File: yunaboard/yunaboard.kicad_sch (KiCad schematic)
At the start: 45 parts, among them J1 USB-C Receptable USB 2.0, J2 JTAG/SWD Tag Connect, J3 PCB ANT, U1 ESP32-S3, U2 CP2102N-Axx-xQFN28, U3 USBLC6-2SC6, U4 MIC5365-3.3YD5, Y1 40 MHz (±10ppm)

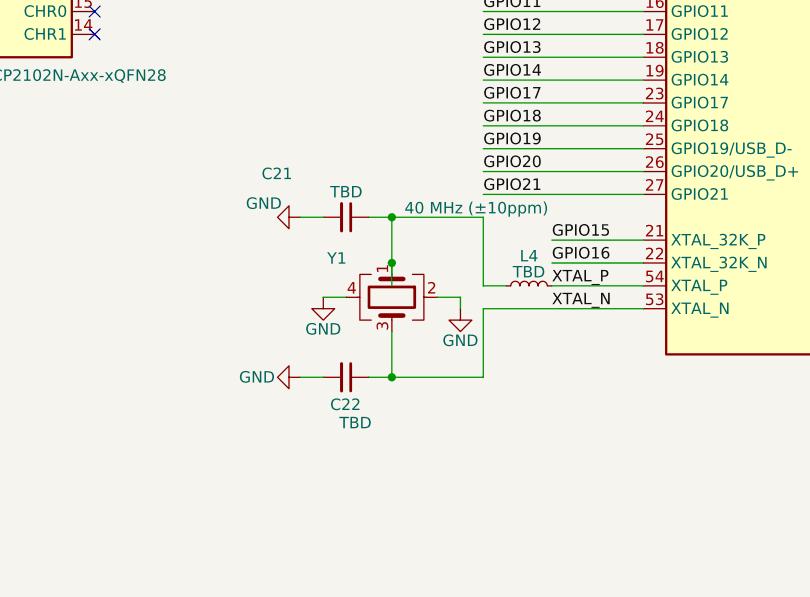
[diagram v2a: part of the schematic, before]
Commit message: Updated
- Added footprints to every component
- Selected capacitors for the external crystals (TBT)
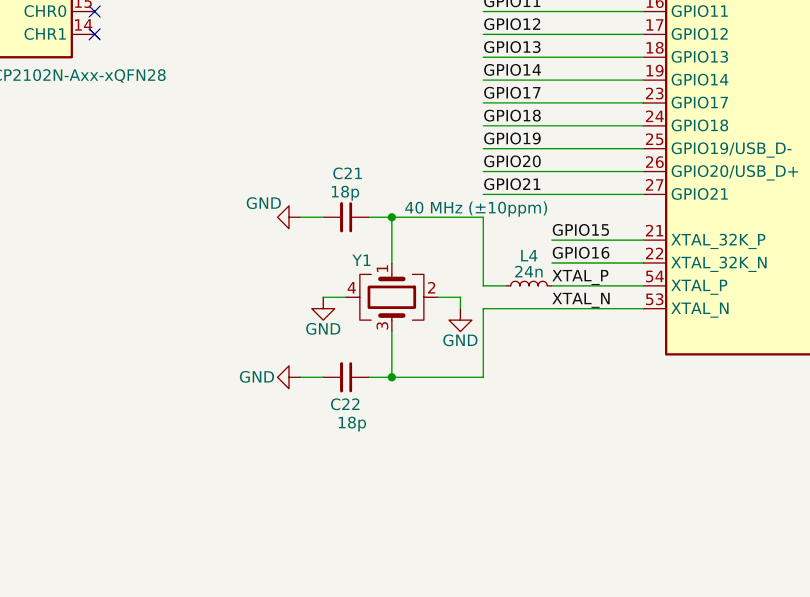
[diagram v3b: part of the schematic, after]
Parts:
- C1, C10, C11, C12, C15, C16, C17, C18, C19, C2, C20, C3, C4, C5, C6: footprint (none) -> Capacitor_SMD:C_0603_1608Metric
- C13, C14, C7, C8, C9: footprint (none) -> Capacitor_SMD:C_0402_1005Metric
- C21, C22: value TBD -> 18p; footprint (none) -> Capacitor_SMD:C_0402_1005Metric
- D1, D2: footprint (none) -> LED_SMD:LED_0603_1608Metric
- J1: footprint (none) -> Connector_USB:USB_C_Receptacle_GCT_USB4105-xx-A_16P_TopMnt_Horizontal
- J3: footprint (none) -> Connector_Coaxial:U.FL_Hirose_U.FL-R-SMT-1_Vertical
- L1, L2, L3: footprint (none) -> Inductor_SMD:L_0201_0603Metric
- L4: value TBD -> 24n; footprint (none) -> Inductor_SMD:L_0201_0603Metric
- R1, R2: footprint (none) -> Resistor_SMD:R_0603_1608Metric
- R3, R4, R5, R6, R7, R8, R9: footprint (none) -> Resistor_SMD:R_0402_1005Metric
- Y1: footprint (none) -> Crystal:Crystal_SMD_3225-4Pin_3.2x2.5mm
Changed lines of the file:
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@@
 	)
 	(junction
-		(at 147.32 127)
-		(diameter 0)
-		(color 0 0 0 0)
-	)
-	(junction
 		(at 33.02 162.56)
 		(diameter 0)
@@
 	(wire
 		(pts
-			(xy 147.32 129.54) (xy 147.32 127)
-		)
-		(stroke
-			(width 0)
-			(type default)
-		)
-	)
-	(wire
-		(pts
 			(xy 45.72 66.04) (xy 48.26 66.04)
 		)
@@
 			)
 		)
-		(property "Footprint" ""
+		(property "Footprint" "Capacitor_SMD:C_0603_1608Metric"
 			(at 142.24 175.26 0)
 			(effects
@@
 			)
 		)
-		(property "Footprint" ""
+		(property "Footprint" "Inductor_SMD:L_0201_0603Metric"
 			(at 137.16 170.18 0)
 			(effects
@@
 			)
 		)
-		(property "Footprint" ""
+		(property "Footprint" "Connector_Coaxial:U.FL_Hirose_U.FL-R-SMT-1_Vertical"
 			(at 165.1 170.18 0)
 			(effects
@@
 			)
 		)
-		(property "Footprint" ""
+		(property "Footprint" "LED_SMD:LED_0603_1608Metric"
 			(at 125.73 73.66 0)
 			(effects
@@
 			)
 		)
-		(property "Footprint" ""
+		(property "Footprint" "Capacitor_SMD:C_0603_1608Metric"
 			(at 187.96 58.42 0)
 			(effects
@@
 			)
 		)
-		(property "Footprint" ""
+		(property "Footprint" "Capacitor_SMD:C_0603_1608Metric"
 			(at 71.12 167.64 0)
 			(effects
@@
 			)
 		)
-		(property "Footprint" ""
+		(property "Footprint" "Capacitor_SMD:C_0603_1608Metric"
 			(at 33.02 167.64 0)
 			(effects
@@
 			)
 		)
-		(property "Footprint" ""
+		(property "Footprint" "Connector_USB:USB_C_Receptacle_GCT_USB4105-xx-A_16P_TopMnt_Horizontal"
 			(at 34.29 73.66 0)
 			(effects
@@
 			)
 		)
-		(property "Footprint" ""
+		(property "Footprint" "Capacitor_SMD:C_0402_1005Metric"
 			(at 180.34 40.64 0)
 			(effects
@@
 		(dnp no)
 		(property "Reference" "Y1"
-			(at 141.224 126.492 90)
+			(at 144.018 126.746 90)
 			(effects
 				(font
@@
 			)
 		)
-		(property "Footprint" ""
+		(property "Footprint" "Crystal:Crystal_SMD_3225-4Pin_3.2x2.5mm"
 			(at 147.32 130.81 0)
 			(effects
@@
 			)
 		)
-		(property "Footprint" ""
+		(property "Footprint" "Capacitor_SMD:C_0402_1005Metric"
 			(at 203.2 35.56 0)
 			(effects
@@
 			)
 		)
-		(property "Footprint" ""
+		(property "Footprint" "Resistor_SMD:R_0603_1608Metric"
 			(at 50.8 63.5 0)
 			(effects
@@
 			)
 		)
-		(property "Footprint" ""
+		(property "Footprint" "Capacitor_SMD:C_0402_1005Metric"
 			(at 220.98 60.96 0)
 			(effects
@@
 			)
 		)
-		(property "Footprint" ""
+		(property "Footprint" "Capacitor_SMD:C_0603_1608Metric"
 			(at 213.36 48.26 0)
 			(effects
@@
 			)
 		)
-		(property "Footprint" ""
+		(property "Footprint" "Capacitor_SMD:C_0402_1005Metric"
 			(at 205.74 48.26 0)
 			(effects
@@
 			)
 		)
-		(property "Footprint" ""
+		(property "Footprint" "Resistor_SMD:R_0402_1005Metric"
 			(at 137.16 73.66 0)
 			(effects
@@
 			)
 		)
-		(property "Footprint" ""
+		(property "Footprint" "Capacitor_SMD:C_0603_1608Metric"
 			(at 152.4 182.88 0)
 			(effects
@@
 			)
 		)
-		(property "Footprint" ""
+		(property "Footprint" "Inductor_SMD:L_0201_0603Metric"
 			(at 152.4 175.26 0)
 			(effects
@@
 			)
 		)
-		(property "Footprint" ""
+		(property "Footprint" "Capacitor_SMD:C_0603_1608Metric"
 			(at 114.3 33.02 0)
 			(effects
@@
 			)
 		)
-		(property "Footprint" ""
+		(property "Footprint" "Capacitor_SMD:C_0603_1608Metric"
 			(at 246.38 139.7 0)
 			(effects
@@
 			)
 		)
-		(property "Footprint" ""
+		(property "Footprint" "Capacitor_SMD:C_0402_1005Metric"
 			(at 190.5 40.64 0)
 			(effects
@@
 			)
 		)
-		(property "Footprint" ""
+		(property "Footprint" "Capacitor_SMD:C_0603_1608Metric"
 			(at 180.34 58.42 0)
 			(effects
@@
 			)
 		)
-		(property "Footprint" ""
+		(property "Footprint" "LED_SMD:LED_0603_1608Metric"
 			(at 125.73 78.74 0)
 			(effects
@@
 			)
 		)
-		(property "Footprint" ""
+		(property "Footprint" "Resistor_SMD:R_0603_1608Metric"
 			(at 50.8 66.04 0)
 			(effects
@@
 			)
 		)
-		(property "Footprint" ""
+		(property "Footprint" "Capacitor_SMD:C_0603_1608Metric"
 			(at 129.54 175.26 0)
 			(effects
@@
 			)
 		)
-		(property "Footprint" ""
+		(property "Footprint" "Capacitor_SMD:C_0603_1608Metric"
 			(at 40.64 167.64 0)
 			(effects
@@
 			)
 		)
-		(property "Footprint" ""
+		(property "Footprint" "Resistor_SMD:R_0402_1005Metric"
 			(at 78.74 45.72 0)
 			(effects
@@
 			)
 		)
-		(property "Footprint" ""
+		(property "Footprint" "Resistor_SMD:R_0402_1005Metric"
 			(at 27.94 162.56 0)
 			(effects
@@
 			)
 		)
-		(property "Value" "TBD"
+		(property "Value" "24n"
 			(at 162.56 128.016 90)
 			(effects
@@
 			)
 		)
-		(property "Footprint" ""
+		(property "Footprint" "Inductor_SMD:L_0201_0603Metric"
 			(at 162.56 129.54 0)
 			(effects
@@
 			)
 		)
-		(property "Footprint" ""
+		(property "Footprint" "Capacitor_SMD:C_0603_1608Metric"
 			(at 175.26 40.64 0)
 			(effects
@@
 			)
 		)
-		(property "Footprint" ""
+		(property "Footprint" "Resistor_SMD:R_0402_1005Metric"
 			(at 246.38 129.54 0)
 			(effects
@@
 			)
 		)
-		(property "Footprint" ""
+		(property "Footprint" "Inductor_SMD:L_0201_0603Metric"
 			(at 185.42 35.56 0)
 			(effects
@@
 			)
 		)
-		(property "Footprint" ""
+		(property "Footprint" "Resistor_SMD:R_0402_1005Metric"
 			(at 137.16 78.74 0)
 			(effects
@@
 			)
 		)
-		(property "Footprint" ""
+		(property "Footprint" "Capacitor_SMD:C_0603_1608Metric"
 			(at 22.86 167.64 0)
 			(effects
@@
 		(dnp no)
 		(property "Reference" "C21"
-			(at 132.842 117.094 90)
+			(at 140.716 117.094 90)
 			(effects
 				(font
@@
 			)
 		)
-		(property "Value" "TBD"
+		(property "Value" "18p"
 			(at 140.462 119.126 90)
 			(effects
@@
 			)
 		)
-		(property "Footprint" ""
+		(property "Footprint" "Capacitor_SMD:C_0402_1005Metric"
 			(at 142.24 121.92 0)
 			(effects
@@
 			)
 		)
-		(property "Footprint" ""
+		(property "Footprint" "Resistor_SMD:R_0402_1005Metric"
 			(at 86.36 40.64 0)
 			(effects
@@
 			)
 		)
-		(property "Value" "TBD"
-			(at 141.478 144.78 90)
+		(property "Value" "18p"
+			(at 141.224 144.78 90)
 			(effects
 				(font
@@
 			)
 		)
-		(property "Footprint" ""
+		(property "Footprint" "Capacitor_SMD:C_0402_1005Metric"
 			(at 142.24 139.7 0)
 			(effects
@@
 			)
 		)
-		(property "Footprint" ""
+		(property "Footprint" "Resistor_SMD:R_0402_1005Metric"
 			(at 78.74 55.88 0)
 			(effects
@@
 			)
 		)
-		(property "Footprint" ""
+		(property "Footprint" "Capacitor_SMD:C_0603_1608Metric"
 			(at 170.18 40.64 0)
 			(effects
@@
 			)
 		)
-		(property "Footprint" ""
+		(property "Footprint" "Capacitor_SMD:C_0603_1608Metric"
 			(at 106.68 33.02 0)
 			(effects

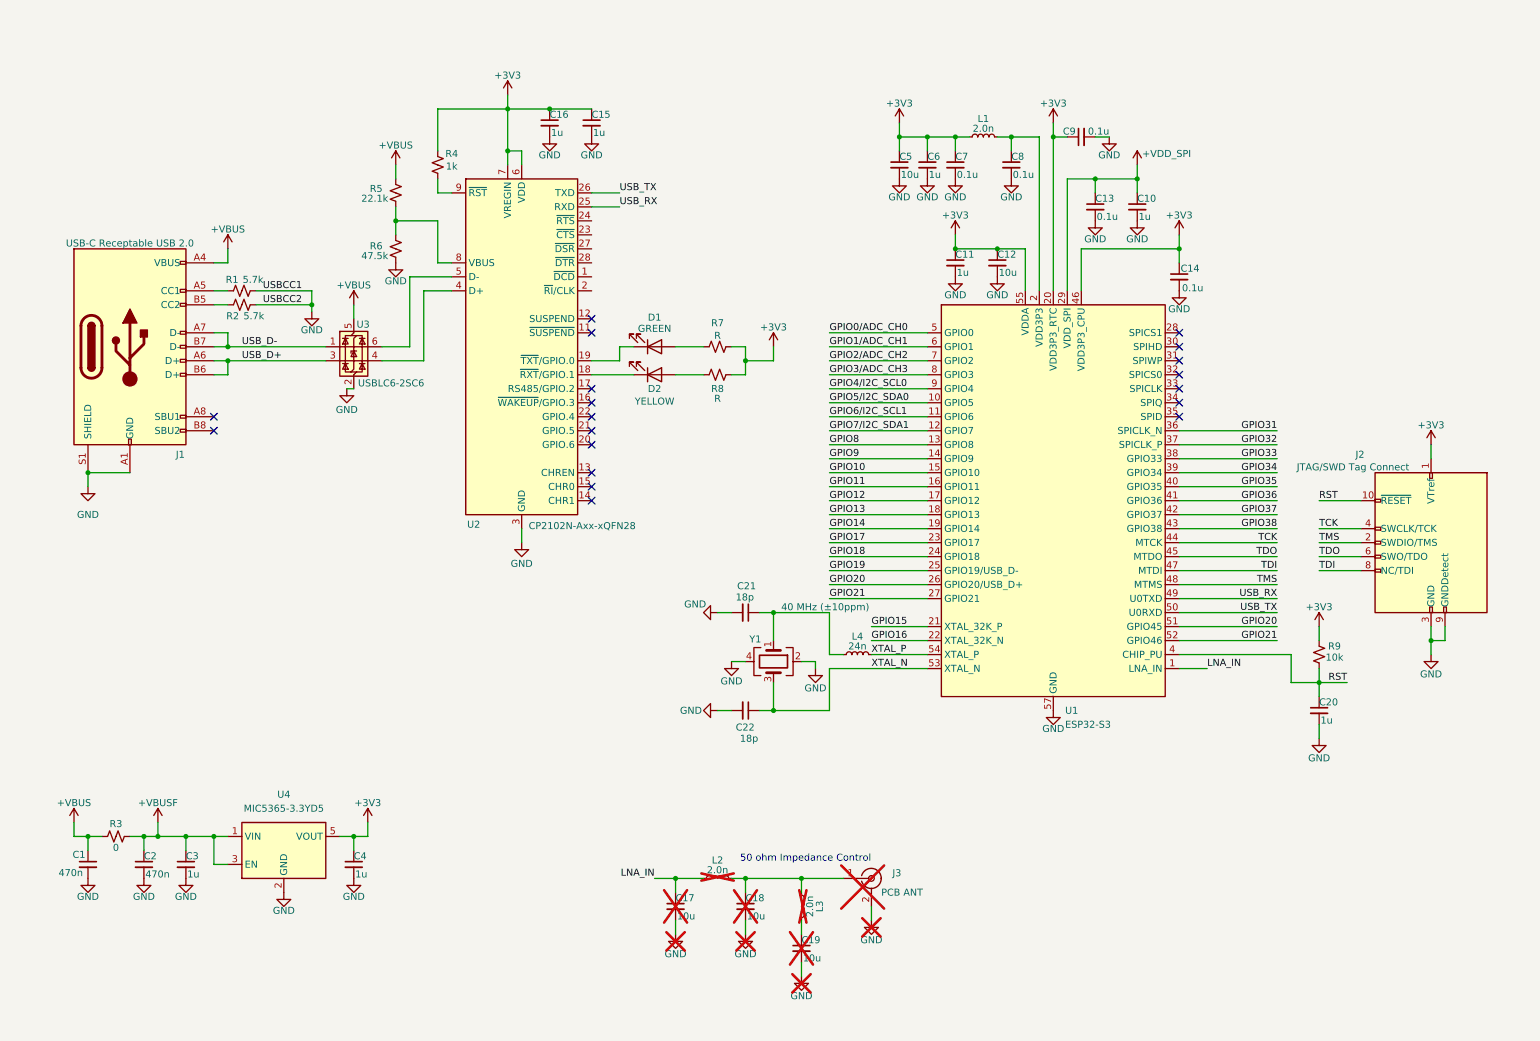
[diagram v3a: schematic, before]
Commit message: Update
- Added GPIO pin headers
- Excluded RF antenna  portion (LNA_IN) - may add in the future
- Started initial PCB layout
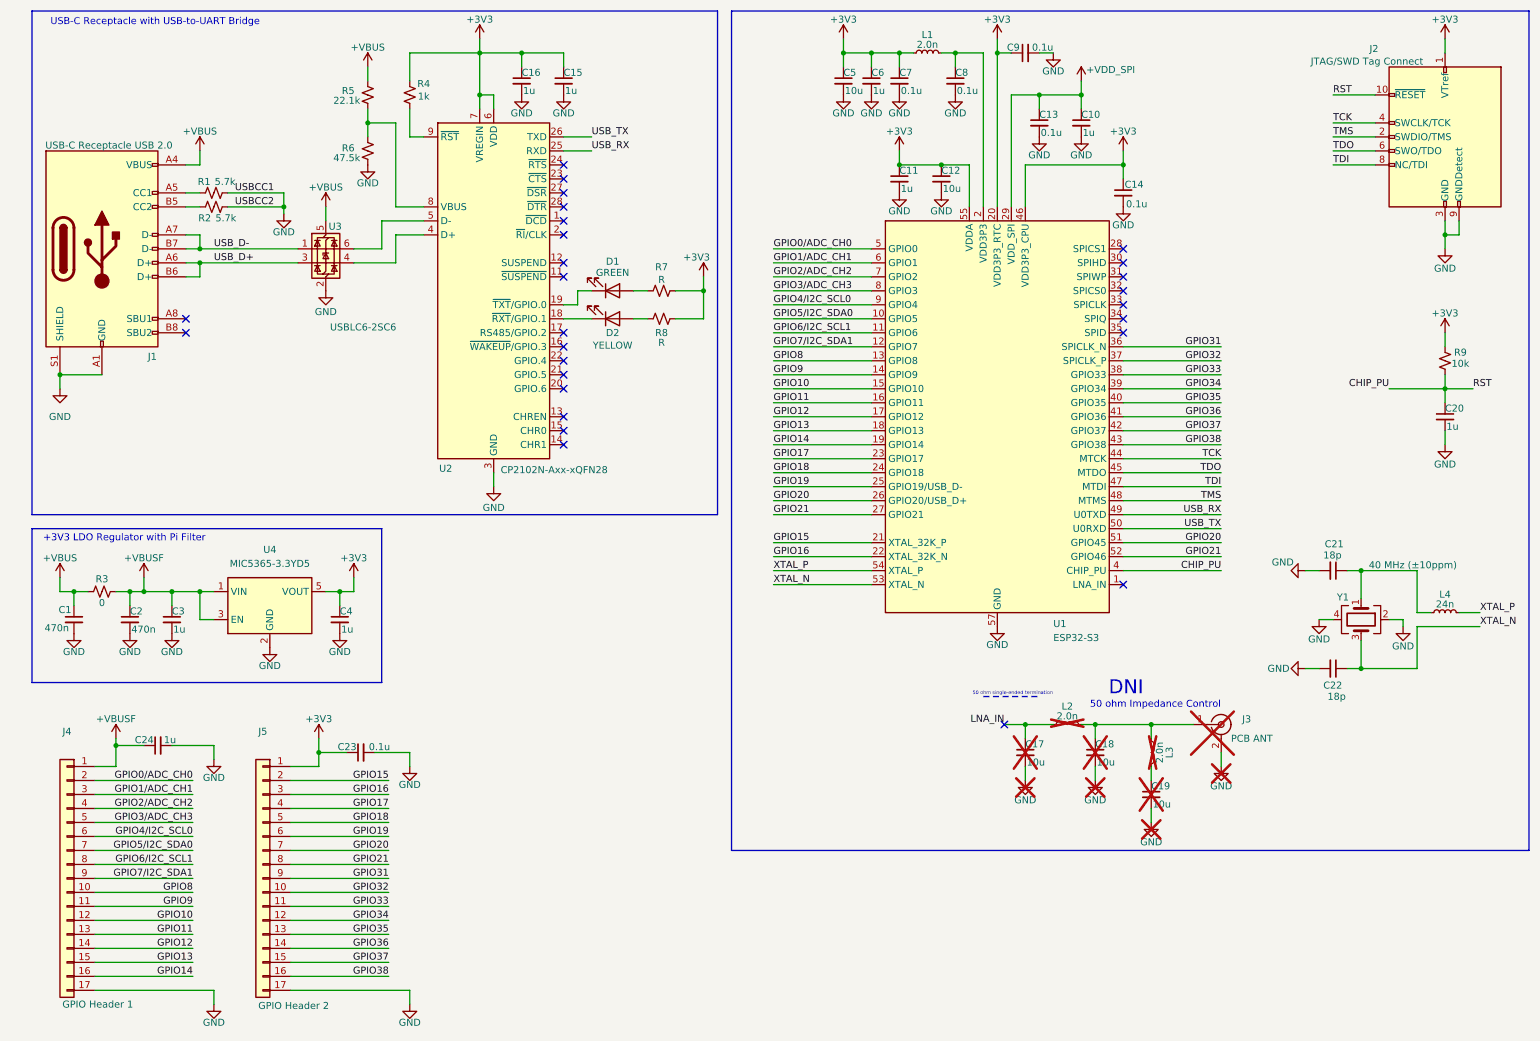
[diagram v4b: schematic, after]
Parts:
- added C23: 0.1u, Capacitor_SMD:C_0402_1005Metric, symbol Device:C_Small
- added C24: 1u, Capacitor_SMD:C_0402_1005Metric, symbol Device:C_Small
- added J4: GPIO Header 1, Connector_PinHeader_1.00mm:PinHeader_1x17_P1.00mm_Vertical, symbol Connector_Generic:Conn_01x17
- added J5: GPIO Header 2, Connector_PinHeader_1.00mm:PinHeader_1x17_P1.00mm_Vertical, symbol Connector_Generic:Conn_01x17
- J1: value USB-C Receptable USB 2.0 -> USB-C Receptacle USB 2.0
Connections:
- net +3V3: now also C23.1, J5.1 (Pin_1)
- net +VBUSF: now also C24.1, J4.1 (Pin_1)
- net GND: now also C23.2, C24.2, J4.17 (Pin_17), J5.17 (Pin_17)
- net GPIO0/ADC_CH0: now also J4.2 (Pin_2)
- net GPIO10: now also J4.12 (Pin_12)
- net GPIO11: now also J4.13 (Pin_13)
- net GPIO12: now also J4.14 (Pin_14)
- net GPIO13: now also J4.15 (Pin_15)
- net GPIO14: now also J4.16 (Pin_16)
- net GPIO15: now also J5.2 (Pin_2)
- net GPIO16: now also J5.3 (Pin_3)
- net GPIO17: now also J5.4 (Pin_4)
- net GPIO18: now also J5.5 (Pin_5)
- net GPIO19: now also J5.6 (Pin_6)
- net GPIO1/ADC_CH1: now also J4.3 (Pin_3)
- net GPIO20: now also J5.7 (Pin_7)
- net GPIO21: now also J5.8 (Pin_8)
- net GPIO2/ADC_CH2: now also J4.4 (Pin_4)
- net GPIO31: now also J5.9 (Pin_9)
- net GPIO32: now also J5.10 (Pin_10)
- net GPIO33: now also J5.11 (Pin_11)
- net GPIO34: now also J5.12 (Pin_12)
- net GPIO35: now also J5.13 (Pin_13)
- net GPIO36: now also J5.14 (Pin_14)
- net GPIO37: now also J5.15 (Pin_15)
- net GPIO38: now also J5.16 (Pin_16)
- net GPIO3/ADC_CH3: now also J4.5 (Pin_5)
- net GPIO4/I2C_SCL0: now also J4.6 (Pin_6)
- net GPIO5/I2C_SDA0: now also J4.7 (Pin_7)
- net GPIO6/I2C_SCL1: now also J4.8 (Pin_8)
- net GPIO7/I2C_SDA1: now also J4.9 (Pin_9)
- net GPIO8: now also J4.10 (Pin_10)
- net GPIO9: now also J4.11 (Pin_11)
- net LNA_IN: no longer U1.1 (LNA_IN)
- net RST renamed CHIP_PU
- no-connect marks 19 -> 27
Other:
- note added: "+3V3 LDO Regulator with Pi Filter"
- note added: "50 ohm single-ended termination"
- note added: "DNI"
- note added: "USB-C Receptacle with USB-to-UART Bridge"
- moved on the sheet: C1, C10, C11, C12, C13, C14, C15, C16, C17, C18, C19, C2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
